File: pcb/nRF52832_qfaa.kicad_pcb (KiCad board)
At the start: 4 copper layers, 41.5 x 13 mm, 87 parts, among them J1 Conn_01x01_Female, J2 Conn_02x05_Odd_Even, U1 NRF52832, U2 W25Q32JVZP, U3 TPS63802DLAR, U4 BQ24078RGTR, U5 RV-4162-C7, U6 SN74LVC1G79DBVT, X1 32.768kHz, X2 32MHz

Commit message: [pcb] updated silkscreen with PCB names
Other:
- board text added: "Dictofun 1.3"
- board text removed: "Dictofun 1.2"
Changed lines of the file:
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@@
       (drillshape 0)
       (scaleselection 1)
-      (outputdirectory "out/v1.3/placement")
+      (outputdirectory "out/v1.3/gerber")
     )
   )
@@
   (gr_arc (start 35.9628 41.8346) (mid 29.4628 35.3346) (end 35.9628 28.8346) (layer "Edge.Cuts") (width 0.05))
   (gr_arc (start 70.878192 39.275374) (mid 68.733663 41.156472) (end 65.9628 41.8346) (layer "Edge.Cuts") (width 0.05))
-  (gr_text "Dictofun 1.2" (at 54.864 34.798) (layer "B.SilkS")
+  (gr_text "Dictofun 1.3" (at 54.864 34.798) (layer "B.SilkS")
     (effects (font (size 1.2 1.2) (thickness 0.3) italic) (justify mirror))
   )
   (gr_text "github.com/rundb/dictofun" (at 43.434 39.37) (layer "B.SilkS")
-    (effects (font (size 1 1) (thickness 0.15)) (justify mirror))
+    (effects (font (size 1 1) (thickness 0.15) italic) (justify mirror))
   )
   (gr_text "ant" (at 42.3418 30.5816) (layer "F.SilkS")

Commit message: start laying out 1.4
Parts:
- removed C14: 0.8pF, Capacitor_SMD:C_0402_1005Metric
- removed C16, C6, C9: 100nF, Capacitor_SMD:C_0402_1005Metric
- removed C22: DNP, Capacitor_SMD:C_0402_1005Metric
- removed C4: 1µF, Capacitor_SMD:C_0402_1005Metric
- removed C5: 4.7µF, Capacitor_SMD:C_0402_1005Metric
- removed C7: 100pF, Capacitor_SMD:C_0402_1005Metric
- removed C8: N.M., Capacitor_SMD:C_0402_1005Metric
- removed D1: ASMB-LTC2-0A335, nRF52832_qfaa:LED_Cree-PLCC4_2x2mm_CW
- removed L2: 3.3nH, Capacitor_SMD:C_0402_1005Metric
- removed RN1: R_Pack04, Resistor_SMD:R_Array_Convex_4x0402
- removed TP11: TestPoint, TestPoint:TestPoint_Pad_D1.0mm
- removed U1: NRF52832, nRF52832_qfaa:QFN40P600X600X90-48_N
- added C28: 100n, Capacitor_SMD:C_0201_0603Metric, F.Cu at (130.8, 94.9)
- added C29: 100n, Capacitor_SMD:C_0201_0603Metric, F.Cu at (139.4, 98.2)
- added C30: 100n, Capacitor_SMD:C_0201_0603Metric, F.Cu at (132.4, 101.8)
- added C31: 100n, Capacitor_SMD:C_0201_0603Metric, F.Cu at (135.2, 101.9)
- added C32: 100n, Capacitor_SMD:C_0201_0603Metric, F.Cu at (132.4, 93.6)
- added C33: 100n, Capacitor_SMD:C_0201_0603Metric, F.Cu at (130.6, 99.3)
- added C34: 100n, Capacitor_SMD:C_0201_0603Metric, F.Cu at (130.6, 97.7)
- added C35: 100n, Capacitor_SMD:C_0201_0603Metric, F.Cu at (130.7, 96.2)
- added C36: N.C, Capacitor_SMD:C_0201_0603Metric, F.Cu at (137.5, 101.9)
- added C37: 1u, Capacitor_SMD:C_0402_1005Metric, F.Cu at (137.5, 93.5)
- added C38: 1u, Capacitor_SMD:C_0402_1005Metric, F.Cu at (139.6, 100.5)
- added C39: 1u, Capacitor_SMD:C_0402_1005Metric, F.Cu at (133.7, 93.0)
- added C39(NP0)1: 100pF, Capacitor_SMD:C_0201_0603Metric, F.Cu at (139.4, 99.7)
- added C40: 1u, Capacitor_SMD:C_0402_1005Metric, F.Cu at (139.5, 97.3)
- added C41: 2.2u, Capacitor_SMD:C_0603_1608Metric, F.Cu at (138.1, 92.2)
- added C42: 4.7u, Capacitor_SMD:C_0603_1608Metric, F.Cu at (141.5, 95.9)
- added C43: 4.7u, Capacitor_SMD:C_0603_1608Metric, F.Cu at (141.5, 92.9)
- added C44: 1u, Capacitor_SMD:C_0402_1005Metric, F.Cu at (139.5, 96.3)
- added C45: 100n, Capacitor_SMD:C_0201_0603Metric, F.Cu at (139.4, 99.0)
- added C46: DNP, Capacitor_SMD:C_0201_0603Metric, F.Cu at (136.7, 104.3)
- added C47: 0.7pF, Capacitor_SMD:C_0201_0603Metric, F.Cu at (135.5, 103.0)
- added D4: ASMB-LTC2-0A335, nRF52832_qfaa:LED_Cree-PLCC4_2x2mm_CW, F.Cu at (124.1, 99.0)
- added J3: USB_B_Micro, Connector_USB:USB_Micro-B_Molex-105017-0001, B.Cu at (152.3, 99.1)
- added J4: Conn_01x02_Socket, _other:SM02B-SRSS-TB_LF__SN_, B.Cu at (149.0, 105.4)
- added J5: Conn_01x03_Socket, _other:JST_SM03B-SRSS-TB_LF__SN_, B.Cu at (148.0, 95.4)
- added L3: 10uH, Inductor_SMD:L_0603_1608Metric, F.Cu at (141.0, 98.7)
- added L4: 10uH, Inductor_SMD:L_0603_1608Metric, F.Cu at (139.2, 94.4)
- added L5: 15nH, Inductor_SMD:L_0201_0603Metric, F.Cu at (136.7, 101.8)
- added L6: 15nH, Inductor_SMD:L_0201_0603Metric, F.Cu at (140.3, 95.0)
- added L7: 2.2nH, Inductor_SMD:L_0201_0603Metric, F.Cu at (135.8, 104.0)
- added R20: 4.7, Resistor_SMD:R_0201_0603Metric, F.Cu at (140.4, 93.1)
- added RN3: R_Pack04, Resistor_SMD:R_Array_Convex_4x0402, F.Cu at (124.0, 96.7)
- added U7: NRF5340-QKAA-R7, _other:XCVR_NRF5340-QKAA-R7, F.Cu at (135.0, 97.5)
- C11, C12: footprint Capacitor_SMD:C_0402_1005Metric -> Capacitor_SMD:C_0201_0603Metric
- TP1, TP10, TP12, TP13, TP14, TP16, TP18, TP19, TP2, TP24, TP25, TP26, TP27, TP28, TP3, TP4, TP5, TP6, TP7, TP8, TP9: moved to F.Cu
- X1: footprint nRF52832_qfaa:XTAL_3215_N -> Crystal:Crystal_SMD_MicroCrystal_CM9V-T1A-2Pin_1.6x1.0mm
- moved TP19 129.9 mm to (136.8, 110.5), turned to 0 degrees
- moved R19 123.0 mm to (143.1, 107.7), turned to -90 degrees
- moved J1 121.7 mm to (135.7, 106.0)
- moved C13 119.2 mm to (138.7, 103.8), turned to 0 degrees
- moved C10 118.7 mm to (141.8, 102.1), turned to -90 degrees
- moved X2 118.3 mm to (139.9, 102.2), turned to 0 degrees
- moved J2 118.1 mm to (131.1, 105.5), turned to -90 degrees
- moved R13 117.4 mm to (140.8, 104.1), turned to 0 degrees
- moved U6 117.0 mm to (140.8, 106.7), turned to 90 degrees
- moved TP28 116.5 mm to (139.8, 110.5), turned to 0 degrees
- moved R17 115.1 mm to (142.9, 105.7), turned to -90 degrees
- moved R1 114.5 mm to (154.3, 101.1), turned to -90 degrees
- moved C20 114.4 mm to (150.3, 103.4), turned to 180 degrees
- moved C3 113.5 mm to (154.3, 98.3), turned to 90 degrees
- moved TP12 113.4 mm to (135.2, 110.5), turned to 0 degrees
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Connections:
- net /P0.00/XL1 renamed Net-(U7C-P0.00/XL1)
- net /P0.01/XL2 renamed Net-(U7C-P0.01/XL2)
- net /P0.28 renamed /PDM_CLK
- net /P0.29 renamed /PDM_DATA
- J2 pad 6: /P0.18/SWO -> /SWO
- R13 pad 1: /P0.25 -> unconnected-(R13-Pad1)
- TP6 pad 1: /P0.12 -> /UART_RX
- TP7 pad 1: /P0.11 -> /UART_TX
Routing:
- net GND: track 132.7 -> 0.00 mm, vias 41 -> 0
- net VCC: track 89.2 -> 0.00 mm, vias 17 -> 0
- net VSS: track 51.1 -> 0.00 mm, vias 8 -> 0
- net FF_CLK: track 34.4 -> 0.00 mm, vias 2 -> 0
- net MAIN_BUTTON: track 33.1 -> 0.00 mm, vias 5 -> 0
- net /Power/FF_D: track 24.8 -> 0.00 mm, vias 2 -> 0
- net /I2C_SCL: track 21.9 -> 0.00 mm, vias 2 -> 0
- net /I2C_SDA: track 21.8 -> 0.00 mm, vias 2 -> 0
- net /SWDCLK: track 19.1 -> 0.00 mm, vias 2 -> 0
- net /SWDIO: track 19.0 -> 0.00 mm, vias 2 -> 0
- net /PDM_DATA: track 17.3 -> 0.00 mm, vias 2 -> 0
- net MCU_POWER_LATCH: track 17.2 -> 0.00 mm, vias 2 -> 0
- net V_charger: track 16.5 -> 0.00 mm, vias 1 -> 0
- net VBAT_LEVEL: track 16.0 -> 0.00 mm, vias 2 -> 0
- net /MEM_CS: track 15.6 -> 0.00 mm, vias 2 -> 0
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- removed copper zone on B.Cu, net GND
- removed copper zone on F.Cu, net GND
- removed copper zone on In1.Cu, net GND
- removed copper zone on F.Cu, net VCC
- removed copper zone on In2.Cu, net VCC
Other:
- board size 41.5 x 13 mm -> 40 x 20 mm
- board text removed: "ant"

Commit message: saving the changes
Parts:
- moved C24 3.80 mm to (125.8, 89.9)
- moved C25 3.80 mm to (127.3, 91.6)
- moved U5 3.80 mm to (125.0, 91.7)
- moved R12 3.80 mm to (123.8, 93.4)
- moved R2 3.80 mm to (122.5, 91.7)
- moved R4 3.80 mm to (123.0, 90.0)
- moved C11 2.91 mm to (133.4, 91.1)
- moved C12 2.91 mm to (131.4, 91.1)
- moved C28 2.91 mm to (127.9, 94.6)
- moved C29 2.91 mm to (136.5, 98.0)
- moved C35 2.91 mm to (127.8, 96.0)
- moved C37 2.91 mm to (134.6, 93.3)
- moved C38 2.91 mm to (136.7, 100.3)
- moved C39(NP0)1 2.91 mm to (136.5, 99.5)
- moved C40 2.91 mm to (136.6, 97.1)
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
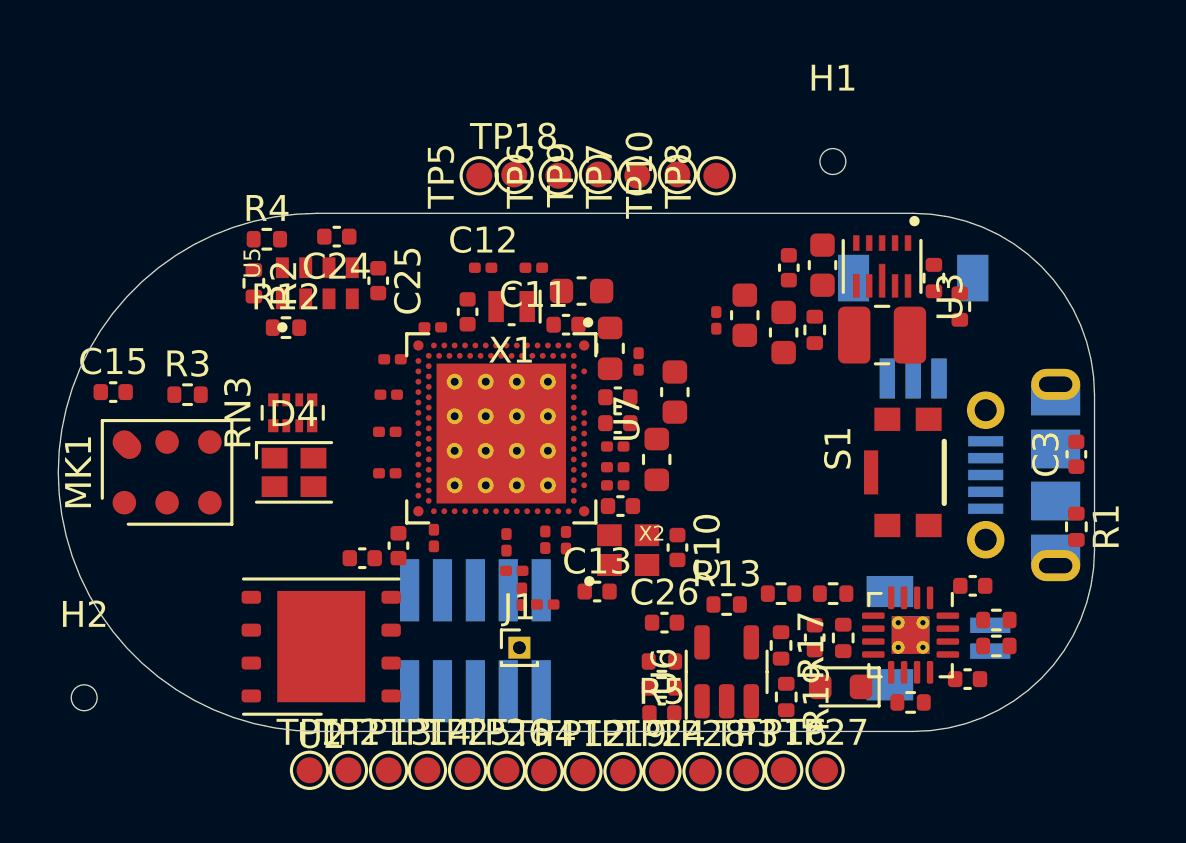
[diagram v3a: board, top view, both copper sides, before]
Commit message: saving changes: layout looks good, most DRC errors are fixed
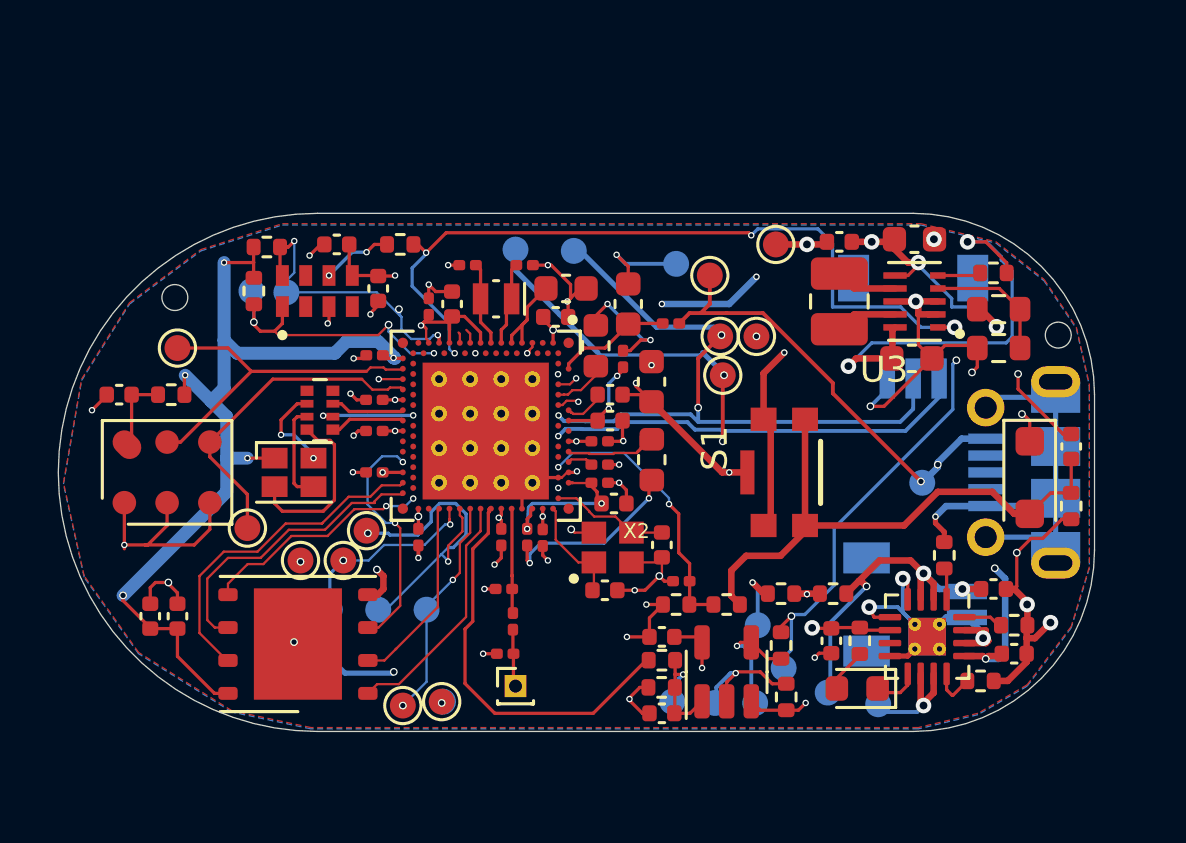
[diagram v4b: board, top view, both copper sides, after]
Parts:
- removed J2: Conn_02x05_Odd_Even, Connector_PinHeader_1.27mm:PinHeader_2x05_P1.27mm_Vertical_SMD
- added C4: 100n, Capacitor_SMD:C_0201_0603Metric, F.Cu at (139.1, 103.2)
- added D5: D_Schottky, Diode_SMD:D_SOD-123F, F.Cu at (152.5, 99.2)
- added R21: 1.6K, Resistor_SMD:R_0402_1005Metric, F.Cu at (138.8, 104.1)
- added TP11: TestPoint, TestPoint:TestPoint_Pad_D1.0mm, B.Cu at (125.5, 104.3)
- added TP15: TestPoint, TestPoint:TestPoint_Pad_D1.0mm, F.Cu at (126.9, 101.2)
- added TP17: TestPoint, TestPoint:TestPoint_Pad_D1.0mm, F.Cu at (128.3, 108.0)
- added TP20: TestPoint, TestPoint:TestPoint_Pad_D1.0mm, F.Cu at (126.0, 102.4)
- added TP21: TestPoint, TestPoint:TestPoint_Pad_D1.0mm, F.Cu at (129.8, 107.8)
- added TP22: TestPoint, TestPoint:TestPoint_Pad_D1.0mm, B.Cu at (123.6, 104.3)
- added TP23: TestPoint, TestPoint:TestPoint_Pad_D1.0mm, B.Cu at (123.6, 106.7)
- added TP29: TestPoint, TestPoint:TestPoint_Pad_D1.0mm, F.Cu at (124.3, 102.4)
- added TP30: TestPoint, TestPoint:TestPoint_Pad_D1.0mm, B.Cu at (134.9, 90.5)
- added TP31: TestPoint, TestPoint:TestPoint_Pad_D1.0mm, B.Cu at (132.7, 90.4)
- MK1: value SPM1423HM4H -> CMM-4737DT
- R12: value 33 -> 330
- R13: value 330 -> 1K
- R15, R16: footprint Resistor_SMD:R_0402_1005Metric -> Resistor_SMD:R_0603_1608Metric
- TP1: value b+ -> TestPoint; moved to B.Cu
- TP12, TP13, TP14, TP16, TP18, TP2, TP24, TP25, TP27, TP28, TP4, TP5: moved to B.Cu
- TP3: value b- -> TestPoint; moved to B.Cu
- moved TP2 24.8 mm to (148.3, 99.4), turned to 180 degrees
- moved TP19 21.2 mm to (142.7, 90.2)
- moved TP26 20.7 mm to (140.2, 91.4)
- moved TP10 20.4 mm to (119.6, 94.2)
- moved TP28 19.6 mm to (138.8, 91.0), turned to 180 degrees
- moved TP9 19.2 mm to (122.3, 101.2)
- moved H2 15.8 mm to (119.5, 92.2)
- moved TP3 13.8 mm to (129.2, 104.3), turned to 180 degrees
- moved TP14 12.9 mm to (141.9, 107.9)
- moved TP13 12.9 mm to (140.3, 107.9)
- moved TP18 11.1 mm to (122.5, 92.0), turned to 180 degrees
- moved H1 11.0 mm to (153.6, 93.7)
- moved TP4 10.00 mm to (142.0, 104.9), turned to 180 degrees
- moved TP6 9.98 mm to (140.7, 95.2)
- moved C17 9.96 mm to (118.5, 104.5)
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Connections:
- C3 pad 1: MAIN_BUTTON -> /BUTTON_INPUT
- J3 pad 1: unconnected-(J3-VBUS-Pad1) -> V_charger
- J3 pad 5: unconnected-(J3-GND-Pad5) -> GND
- J3 pad 6: unconnected-(J3-Shield-Pad6) -> GND
- J5 pad 2: /Power/DBG_TX -> /DBG_TX
- J5 pad 3: /Power/DBG_RX -> /DBG_RX
- R1 pad 1: MAIN_BUTTON -> /BUTTON_INPUT
- R12 pad 1: /RTC_INT_N -> VREG_EN
- R13 pad 1: unconnected-(R13-Pad1) -> /BUTTON_INPUT_MCU
- R13 pad 2: MAIN_BUTTON -> /BUTTON_INPUT
- R15 pad 1: VCC -> Net-(U3-FB)
- R15 pad 2: Net-(U3-FB) -> VCC
- R17 pad 1: MAIN_BUTTON -> VREG_EN
- R20 pad 1: VBUS -> V_charger
- S1 pad 2: MAIN_BUTTON -> /BUTTON_INPUT
- S1 pad 3: MAIN_BUTTON -> /BUTTON_INPUT
- TP1 pad 1: +BATT -> /SWDIO
- TP16 pad 1: MAIN_BUTTON -> VREG_EN
- TP3 pad 1: GND -> /SWDCLK
- TP6 pad 1: /UART_RX -> /DBG_RX
- TP7 pad 1: /UART_TX -> /DBG_TX
- U3 pad 1: MAIN_BUTTON -> VREG_EN
- U7 pad AB2: unconnected-(U7C-P0.06/AIN2-PadAB2) -> VREG_EN
- U7 pad AE1: unconnected-(U7D-P1.02/TWI-PadAE1) -> /I2C_SCL
- U7 pad AE31: unconnected-(U7C-P0.28/AIN7-PadAE31) -> /MEM_DO
- U7 pad AF2: unconnected-(U7D-P1.03/TWI-PadAF2) -> /I2C_SDA
- U7 pad AK14: unconnected-(U7C-P0.18/CSN-PadAK14) -> /LED_BLUE
- U7 pad AK30: unconnected-(U7C-P0.27/AIN6-PadAK30) -> /MEM_DI
- U7 pad AL13: unconnected-(U7C-P0.19-PadAL13) -> /LED_RED
- U7 pad AL15: unconnected-(U7C-P0.21-PadAL15) -> /LED_GREEN
- U7 pad AL23: unconnected-(U7D-P1.08-PadAL23) -> /MEM_IO2
- U7 pad AL27: unconnected-(U7C-P0.24-PadAL27) -> /MEM_IO3
- U7 pad AL29: unconnected-(U7C-P0.26/AIN5-PadAL29) -> /MEM_CLK
- U7 pad AL5: unconnected-(U7C-P0.13/IO[0]-PadAL5) -> /PDM_DATA
- U7 pad AL9: unconnected-(U7C-P0.16/IO[3]-PadAL9) -> /PDM_CLK
- U7 pad B14: unconnected-(U7D-P1.15-PadB14) -> /DBG_TX
- U7 pad B18: unconnected-(U7D-P1.12-PadB18) -> /DBG_RX
- U7 pad B24: unconnected-(U7C-P0.30-PadB24) -> /BUTTON_INPUT_MCU
- U7 pad R31: unconnected-(U7D-P1.10-PadR31) -> MCU_POWER_LATCH
- U7 pad U31: unconnected-(U7C-P0.29-PadU31) -> /MEM_CS
- U7 pad V2: unconnected-(U7C-P0.04/AIN0-PadV2) -> VBAT_LEVEL
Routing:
- net GND: track 0.00 -> 254.5 mm, vias 0 -> 54
- net VCC: track 0.00 -> 129.7 mm, vias 0 -> 24
- net VSS: track 0.00 -> 84.4 mm, vias 0 -> 7
- net VREG_EN: track 0.00 -> 52.6 mm, vias 0 -> 7
- net /DBG_RX: track 0.00 -> 30.0 mm, vias 0 -> 3
- net V_charger: track 0.00 -> 28.4 mm, vias 0 -> 4
- net /DBG_TX: track 0.00 -> 26.1 mm, vias 0 -> 3
- net VBAT_LEVEL: track 0.00 -> 23.0 mm, vias 0 -> 2
- net /BUTTON_INPUT: track 0.00 -> 22.1 mm
- net MCU_POWER_LATCH: track 0.00 -> 15.8 mm
- net +BATT: track 0.00 -> 13.9 mm, vias 0 -> 3
- net /PDM_DATA: track 0.00 -> 13.6 mm
- net /MEM_IO3: track 0.00 -> 13.1 mm
- net /SWDIO: track 0.00 -> 12.8 mm, vias 0 -> 2
- net /PDM_CLK: track 0.00 -> 12.6 mm
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- added copper zone on F.Cu, net GND
- added copper zone on In1.Cu, net GND
- added copper zone on B.Cu, net VCC
- added copper zone on In2.Cu, net VCC

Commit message: finalizing 1.4, going for the dry run
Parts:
- added C5: 100n, Capacitor_SMD:C_0201_0603Metric, F.Cu at (147.7, 96.5)
- added C6: 1u, Capacitor_SMD:C_0402_1005Metric, F.Cu at (148.6, 96.4)
- added C7: 100n, Capacitor_SMD:C_0201_0603Metric, F.Cu at (147.0, 96.5)
- added C8: 100n, Capacitor_SMD:C_0201_0603Metric, F.Cu at (150.5, 98.9)
- added D1: PRTR5V0U2X, Package_TO_SOT_SMD:SOT-143, F.Cu at (148.2, 99.8)
- added FB1: FerriteBead, Inductor_SMD:L_0402_1005Metric, F.Cu at (148.2, 97.8)
- added FB2: FerriteBead, Inductor_SMD:L_0402_1005Metric, F.Cu at (150.5, 98.0)
- added FB3: FerriteBead, Inductor_SMD:L_0402_1005Metric, F.Cu at (148.8, 101.8)
- added Q1: PMOS, Package_TO_SOT_SMD:SOT-23, F.Cu at (120.4, 92.7)
- added R22: 4.7k, Resistor_SMD:R_0402_1005Metric, F.Cu at (150.7, 99.8)
- added R23: 1M, Resistor_SMD:R_0402_1005Metric, F.Cu at (123.2, 94.1)
- added R24: 100K, Resistor_SMD:R_0402_1005Metric, F.Cu at (122.3, 95.2)
- added TP32: TestPoint, TestPoint:TestPoint_Pad_D1.0mm, B.Cu at (126.9, 91.5)
- U2: value W25Q32JVZP -> W25Q128JWPIQ
- moved TP2 11.6 mm to (141.0, 90.4)
- moved H2 7.72 mm to (116.0, 99.1)
- moved TP10 1.94 mm to (117.7, 94.4)
- moved L6 1.78 mm to (138.4, 95.4)
- moved C42 1.74 mm to (137.6, 93.8), turned to 0 degrees
- moved L4 1.26 mm to (136.7, 95.0), turned to 180 degrees
- moved C43 1.17 mm to (137.4, 91.4), turned to 180 degrees
- moved R20 0.87 mm to (139.4, 92.8)
- moved R7 0.73 mm to (149.7, 102.8), turned to 0 degrees
- moved TP5 0.45 mm to (124.2, 92.0)
- moved L3 0.23 mm to (138.1, 98.5)
- moved H1 0.20 mm to (153.4, 93.7)
- moved C20 0.13 mm to (151.1, 103.6)
- moved C44 0.07 mm to (136.3, 96.1)
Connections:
- J3 pad 1: V_charger -> Net-(J3-VBUS)
- J3 pad 2: unconnected-(J3-D--Pad2) -> /USB_N
- J3 pad 3: unconnected-(J3-D+-Pad3) -> /USB_P
- J3 pad 5: GND -> Net-(J3-GND)
- J3 pad 6: GND -> Net-(J3-Shield)
- R12 pad 1: VREG_EN -> /RTC_INT_N
- U7 pad AB2: VREG_EN -> /RTC_INT_N
- U7 pad B2: unconnected-(U7B-D+-PadB2) -> /USB_P
- U7 pad B4: unconnected-(U7B-D--PadB4) -> /USB_N
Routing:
- net /USB_N: track 0.00 -> 27.9 mm, vias 0 -> 3
- net /USB_P: track 0.00 -> 21.4 mm, vias 0 -> 2
- net Net-(J3-Shield): track 0.00 -> 18.3 mm
- net /RTC_INT_N: track 0.00 -> 17.9 mm, vias 0 -> 4
- net GND: track 254.5 -> 271.0 mm, vias 54 -> 59
- net VREG_EN: track 52.6 -> 61.9 mm
- net VSS: track 84.4 -> 91.5 mm, vias 7 -> 8
- net Net-(J3-VBUS): track 0.00 -> 4.16 mm, vias 0 -> 1
- net /PDM_DATA: track 13.6 -> 17.4 mm
- net Net-(U7A-VBUS): track 4.48 -> 8.08 mm, vias 0 -> 3
- net Net-(L4-Pad1): track 4.57 -> 1.03 mm, vias 2 -> 0
- net VCC: track 129.7 -> 132.8 mm
- net Net-(J3-GND): track 0.00 -> 2.75 mm, vias 0 -> 1
- net V_charger: track 28.4 -> 30.2 mm, vias 4 -> 5
- net Net-(U7A-DECD): track 3.45 -> 5.15 mm
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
